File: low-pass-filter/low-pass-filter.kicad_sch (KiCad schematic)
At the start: 32 parts, among them J1 Input Jack, J2 Output Jack, Q1 PNP, Q2 PNP, U1 LM13700, U2 TL074

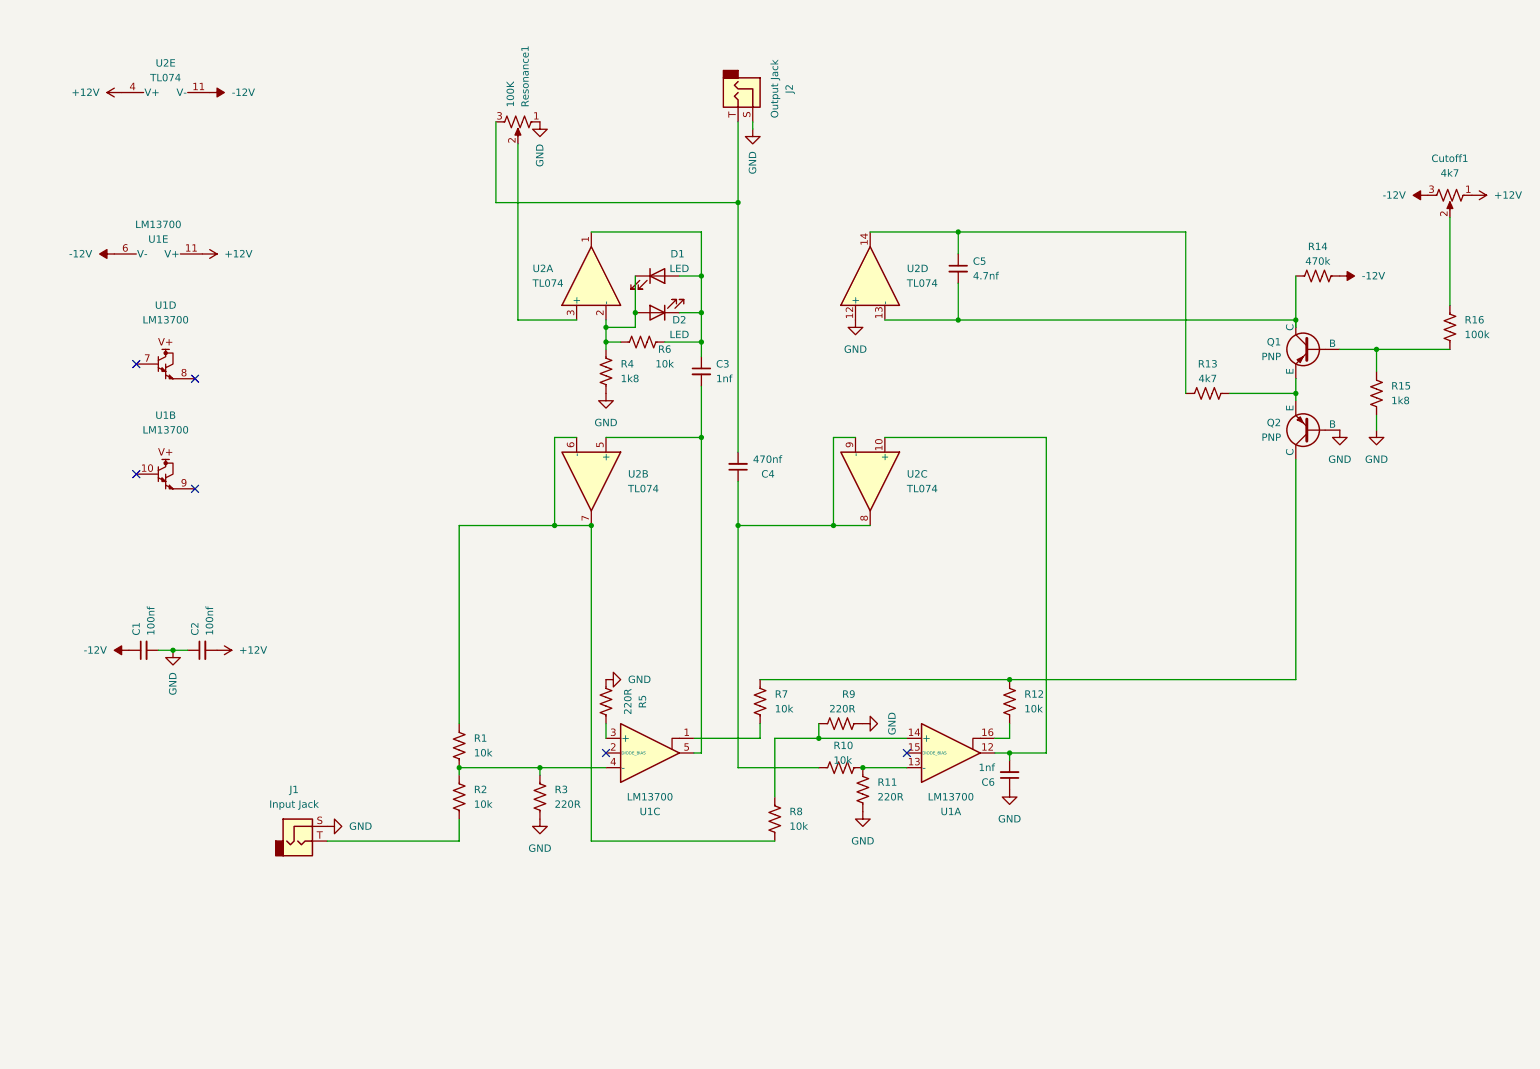
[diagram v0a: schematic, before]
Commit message: Tidy up low-pass filter schematic
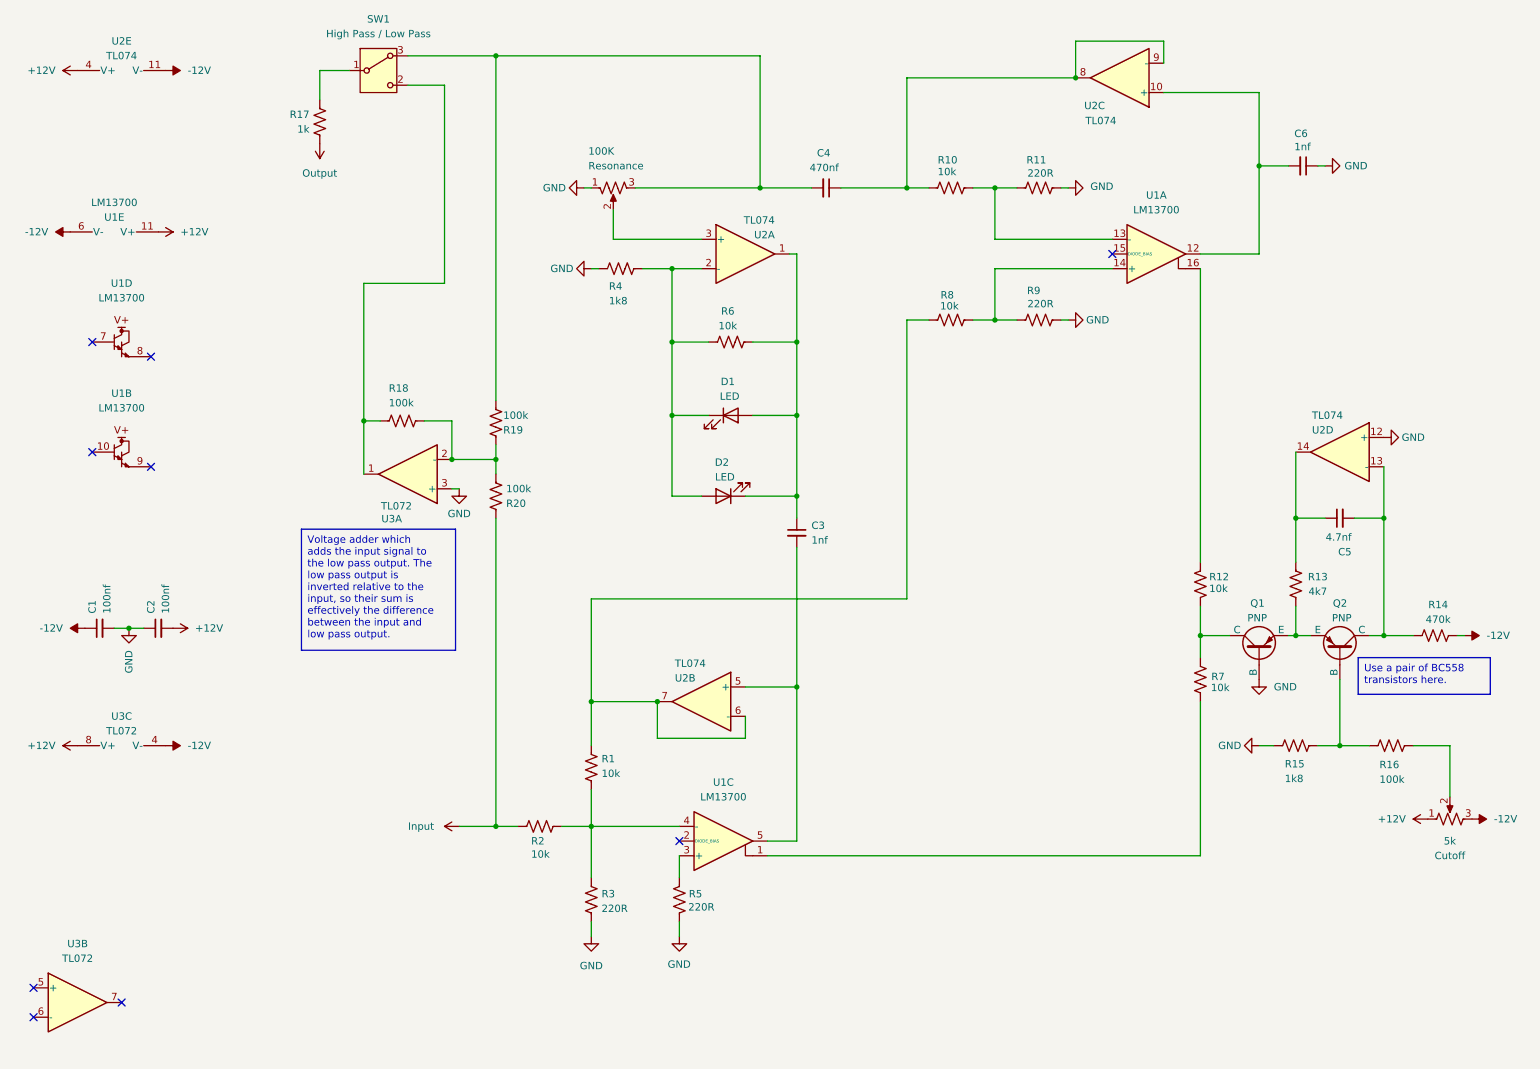
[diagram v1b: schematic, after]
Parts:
- removed J1: Input Jack, symbol Connector_Audio:AudioJack2
- removed J2: Output Jack, symbol Connector_Audio:AudioJack2
- added R17: 1k, symbol Device:R_US
- added R18, R19, R20: 100k, symbol Device:R_US
- added SW1: High Pass / Low Pass, symbol Switch:SW_SPDT_312
- added U3: TL072, symbol Amplifier_Operational:TL072
- Cutoff: renamed from Cutoff1; value 4k7 -> 5k
- renumbered Resonance1 to Resonance
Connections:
- net +12V: now also U3.8 (V+)
- net -12V: now also R14.2, U3.4 (V-); no longer R14.1
- net GND: now also U3.3 (+)
- net at R1.1, U2.6 (-), U2.7: now also R8.1; no longer R8.2
- net at R9.1, U1.14 (+): now also R8.2; no longer R8.1
- net at C4.2, Resonance.3: now also R19.1, SW1.3 (A)
- net at C5.2, Q1.1 (C), U2.13 (-): now also R14.1; no longer R14.2
- net Input: now reaches R2.2
- net Input: now also R20.2
- new net: R18.1, R19.2, R20.1, U3.2 (-)
- new net: R18.2, SW1.2 (C), U3.1
- new net: R17.2, SW1.1 (B)
- new net Output: R17.1
- no-connect marks 6 -> 9
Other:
- moved on the sheet: C1, C2, C3, C4, C5, C6, Cutoff, D1, D2, Q1, Q2, R1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

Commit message: Update low pass filter
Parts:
- added CVLevel: 100K, symbol Device:R_Potentiometer_US
- added R21: 100k, symbol Device:R_US
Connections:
- net GND: now also CVLevel.1
- net Output: now also R17.2; no longer R17.1
- net at SW1.1 (B): now also R17.1; no longer R17.2
- net at Q1.2 (B), R15.2, R16.1: now also R21.2
- new net: CVLevel.2, R21.1
- new net CV: CVLevel.3
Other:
- moved on the sheet: C5, Cutoff, Q1, Q2, R12, R13, R14, R15, R16, R17, R7, SW1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

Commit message: Maybe fix bug in low-pass filter
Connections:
- net at C4.2, R19.1, Resonance.3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: now also R10.2
- net at C4.1, U2.8, U2.9 (-): no longer R10.2
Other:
- moved on the sheet: C4
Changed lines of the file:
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@@
 	)
 	(junction
-		(at 143.51 44.45)
-		(diameter 0)
-		(color 0 0 0 0)
-	)
-	(junction
 		(at 236.22 115.57)
 		(diameter 0)
@@
 	)
 	(junction
-		(at 168.91 44.45)
-		(diameter 0)
-		(color 0 0 0 0)
-	)
-	(junction
 		(at 229.87 40.64)
 		(diameter 0)
@@
 	)
 	(junction
+		(at 143.51 44.45)
+		(diameter 0)
+		(color 0 0 0 0)
+	)
+	(junction
 		(at 97.79 44.45)
 		(diameter 0)
@@
 	)
 	(junction
+		(at 168.91 44.45)
+		(diameter 0)
+		(color 0 0 0 0)
+	)
+	(junction
 		(at 90.17 91.44)
 		(diameter 0)
@@
 	(wire
 		(pts
+			(xy 168.91 44.45) (xy 172.72 44.45)
+		)
+		(stroke
+			(width 0)
+			(type default)
+		)
+	)
+	(wire
+		(pts
 			(xy 149.86 106.68) (xy 149.86 130.81)
 		)
@@
 	(wire
 		(pts
-			(xy 168.91 44.45) (xy 157.48 44.45)
-		)
-		(stroke
-			(width 0)
-			(type default)
-		)
-	)
-	(wire
-		(pts
 			(xy 129.54 173.99) (xy 129.54 171.45)
 		)
@@
 	(wire
 		(pts
-			(xy 168.91 44.45) (xy 172.72 44.45)
+			(xy 168.91 36.83) (xy 168.91 44.45)
+		)
+		(stroke
+			(width 0)
+			(type default)
+		)
+	)
+	(wire
+		(pts
+			(xy 143.51 44.45) (xy 168.91 44.45)
 		)
 		(stroke
@@
 	(wire
 		(pts
-			(xy 213.36 19.05) (xy 198.12 19.05)
+			(xy 168.91 25.4) (xy 168.91 31.75)
 		)
 		(stroke
@@
 	(wire
 		(pts
-			(xy 236.22 83.82) (xy 236.22 95.25)
+			(xy 213.36 19.05) (xy 198.12 19.05)
 		)
 		(stroke
@@
 	(wire
 		(pts
-			(xy 219.71 115.57) (xy 224.79 115.57)
+			(xy 236.22 83.82) (xy 236.22 95.25)
 		)
 		(stroke
@@
 	(wire
 		(pts
-			(xy 36.83 120.65) (xy 34.29 120.65)
+			(xy 219.71 115.57) (xy 224.79 115.57)
 		)
 		(stroke
@@
 	(wire
 		(pts
-			(xy 243.84 143.51) (xy 243.84 140.97)
+			(xy 36.83 120.65) (xy 34.29 120.65)
 		)
 		(stroke
@@
 	(wire
 		(pts
-			(xy 184.15 44.45) (xy 187.96 44.45)
+			(xy 243.84 143.51) (xy 243.84 140.97)
 		)
 		(stroke
@@
 	(wire
 		(pts
-			(xy 34.29 120.65) (xy 31.75 120.65)
+			(xy 184.15 44.45) (xy 187.96 44.45)
 		)
 		(stroke
@@
 	(wire
 		(pts
-			(xy 128.27 97.79) (xy 133.35 97.79)
+			(xy 34.29 120.65) (xy 31.75 120.65)
 		)
 		(stroke
@@
 	(wire
 		(pts
-			(xy 143.51 44.45) (xy 152.4 44.45)
+			(xy 128.27 97.79) (xy 133.35 97.79)
 		)
 		(stroke
@@
 	(wire
 		(pts
-			(xy 168.91 25.4) (xy 168.91 44.45)
-		)
-		(stroke
-			(width 0)
-			(type default)
-		)
-	)
-	(wire
-		(pts
 			(xy 97.79 88.9) (xy 97.79 91.44)
 		)
@@
 		)
 		(instances
-			(project ""
+			(project "low-pass-filter"
 				(path "/e72ee090-6f9b-4823-9ab6-f31beee51bd1"
 					(reference "U3")
@@
 		)
 		(instances
-			(project ""
+			(project "low-pass-filter"
 				(path "/e72ee090-6f9b-4823-9ab6-f31beee51bd1"
 					(reference "U3")
@@
 	(symbol
 		(lib_id "Device:C_Small")
-		(at 154.94 44.45 270)
+		(at 168.91 34.29 0)
 		(unit 1)
 		(exclude_from_sim no)
@@
 		(dnp no)
 		(property "Reference" "C4"
-			(at 153.3525 38.4175 90)
+			(at 163.576 33.528 0)
 			(effects
 				(font
@@
 		)
 		(property "Value" "470nf"
-			(at 152.0825 40.9575 90)
+			(at 160.782 36.068 0)
 			(effects
 				(font
@@
 		)
 		(property "Footprint" ""
-			(at 154.94 44.45 0)
+			(at 168.91 34.29 0)
 			(effects
 				(font
@@
 		)
 		(property "Datasheet" "~"
-			(at 154.94 44.45 0)
+			(at 168.91 34.29 0)
 			(effects
 				(font
@@
 		)
 		(property "Description" ""
-			(at 154.94 44.45 0)
+			(at 168.91 34.29 0)
 			(effects
 				(font
@@
 		)
 		(instances
-			(project ""
+			(project "low-pass-filter"
 				(path "/e72ee090-6f9b-4823-9ab6-f31beee51bd1"
 					(reference "SW1")
@@
 		)
 		(instances
-			(project ""
+			(project "low-pass-filter"
 				(path "/e72ee090-6f9b-4823-9ab6-f31beee51bd1"
 					(reference "#PWR023")
@@
 		)
 		(instances
-			(project ""
+			(project "low-pass-filter"
 				(path "/e72ee090-6f9b-4823-9ab6-f31beee51bd1"
 					(reference "U3")

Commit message: Revert "Maybe fix bug in low-pass filter"
It was right the first time.

This reverts commit b62497d0d33f661917a797e78c2c214d61ac51a2.
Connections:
- net at C4.2, R19.1, Resonance.3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: no longer R10.2
- net at C4.1, U2.8, U2.9 (-): now also R10.2
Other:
- moved on the sheet: C4
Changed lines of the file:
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@@
 	)
 	(junction
+		(at 143.51 44.45)
+		(diameter 0)
+		(color 0 0 0 0)
+	)
+	(junction
 		(at 236.22 115.57)
 		(diameter 0)
@@
 	)
 	(junction
+		(at 168.91 44.45)
+		(diameter 0)
+		(color 0 0 0 0)
+	)
+	(junction
 		(at 229.87 40.64)
 		(diameter 0)
@@
 	)
 	(junction
-		(at 143.51 44.45)
-		(diameter 0)
-		(color 0 0 0 0)
-	)
-	(junction
 		(at 97.79 44.45)
 		(diameter 0)
@@
 	)
 	(junction
-		(at 168.91 44.45)
-		(diameter 0)
-		(color 0 0 0 0)
-	)
-	(junction
 		(at 90.17 91.44)
 		(diameter 0)
@@
 	(wire
 		(pts
-			(xy 168.91 44.45) (xy 172.72 44.45)
-		)
-		(stroke
-			(width 0)
-			(type default)
-		)
-	)
-	(wire
-		(pts
 			(xy 149.86 106.68) (xy 149.86 130.81)
 		)
@@
 	(wire
 		(pts
+			(xy 168.91 44.45) (xy 157.48 44.45)
+		)
+		(stroke
+			(width 0)
+			(type default)
+		)
+	)
+	(wire
+		(pts
 			(xy 129.54 173.99) (xy 129.54 171.45)
 		)
@@
 	(wire
 		(pts
-			(xy 168.91 36.83) (xy 168.91 44.45)
-		)
-		(stroke
-			(width 0)
-			(type default)
-		)
-	)
-	(wire
-		(pts
-			(xy 143.51 44.45) (xy 168.91 44.45)
+			(xy 168.91 44.45) (xy 172.72 44.45)
 		)
 		(stroke
@@
 	(wire
 		(pts
-			(xy 168.91 25.4) (xy 168.91 31.75)
-		)
-		(stroke
-			(width 0)
-			(type default)
-		)
-	)
-	(wire
-		(pts
 			(xy 213.36 19.05) (xy 198.12 19.05)
 		)
@@
 	(wire
 		(pts
+			(xy 143.51 44.45) (xy 152.4 44.45)
+		)
+		(stroke
+			(width 0)
+			(type default)
+		)
+	)
+	(wire
+		(pts
 			(xy 74.93 60.96) (xy 74.93 84.7725)
 		)
@@
 	(wire
 		(pts
+			(xy 168.91 25.4) (xy 168.91 44.45)
+		)
+		(stroke
+			(width 0)
+			(type default)
+		)
+	)
+	(wire
+		(pts
 			(xy 97.79 88.9) (xy 97.79 91.44)
 		)
@@
 		)
 		(instances
-			(project "low-pass-filter"
+			(project ""
 				(path "/e72ee090-6f9b-4823-9ab6-f31beee51bd1"
 					(reference "U3")
@@
 		)
 		(instances
-			(project "low-pass-filter"
+			(project ""
 				(path "/e72ee090-6f9b-4823-9ab6-f31beee51bd1"
 					(reference "U3")
@@
 	(symbol
 		(lib_id "Device:C_Small")
-		(at 168.91 34.29 0)
+		(at 154.94 44.45 270)
 		(unit 1)
 		(exclude_from_sim no)
@@
 		(dnp no)
 		(property "Reference" "C4"
-			(at 163.576 33.528 0)
+			(at 153.3525 38.4175 90)
 			(effects
 				(font
@@
 		)
 		(property "Value" "470nf"
-			(at 160.782 36.068 0)
+			(at 152.0825 40.9575 90)
 			(effects
 				(font
@@
 		)
 		(property "Footprint" ""
-			(at 168.91 34.29 0)
+			(at 154.94 44.45 0)
 			(effects
 				(font
@@
 		)
 		(property "Datasheet" "~"
-			(at 168.91 34.29 0)
+			(at 154.94 44.45 0)
 			(effects
 				(font
@@
 		)
 		(property "Description" ""
-			(at 168.91 34.29 0)
+			(at 154.94 44.45 0)
 			(effects
 				(font
@@
 		)
 		(instances
-			(project "low-pass-filter"
+			(project ""
 				(path "/e72ee090-6f9b-4823-9ab6-f31beee51bd1"
 					(reference "SW1")
@@
 		)
 		(instances
-			(project "low-pass-filter"
+			(project ""
 				(path "/e72ee090-6f9b-4823-9ab6-f31beee51bd1"
 					(reference "#PWR023")
@@
 		)
 		(instances
-			(project "low-pass-filter"
+			(project ""
 				(path "/e72ee090-6f9b-4823-9ab6-f31beee51bd1"
 					(reference "U3")
